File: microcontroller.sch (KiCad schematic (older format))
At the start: 15 parts

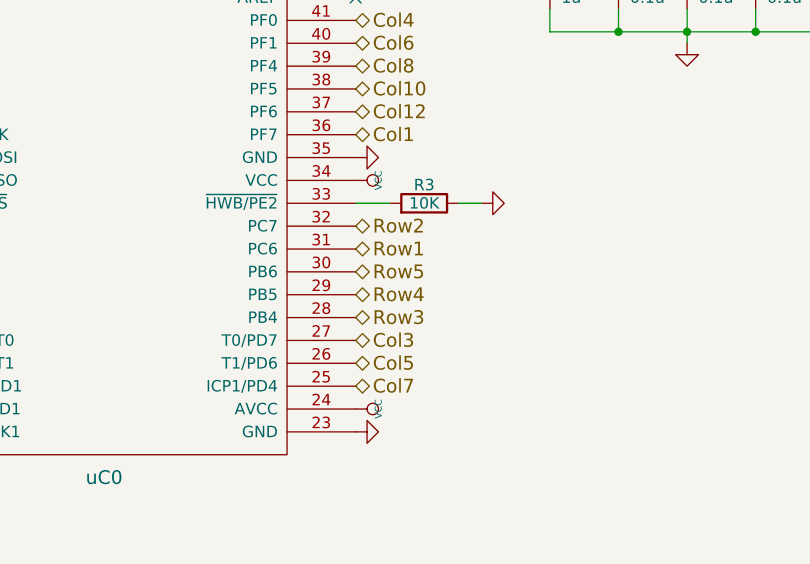
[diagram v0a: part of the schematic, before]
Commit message: Branch for finalizing the board.
TODO:
Swap to smaller components, finalize pads
Added footprints.pretty
Add RGB underglow
Added schematic library (keenkeeb.lib/dcm)
Remove SPI header (?)
Add test pads (?)
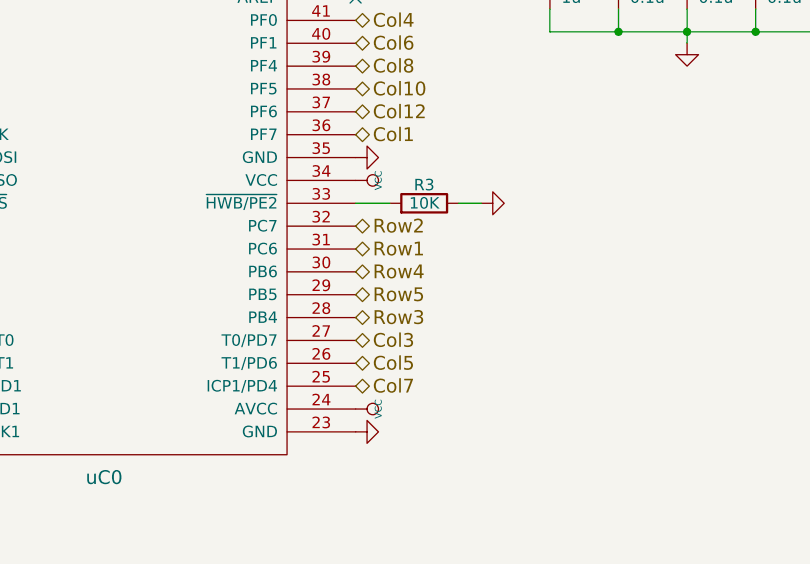
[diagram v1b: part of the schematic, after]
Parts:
- C0, C1, C2, C3, C4, C5, C6, C7: footprint Capacitors_SMD:C_0805_HandSoldering -> Capacitors_SMD:C_0805
- OSC0: footprint keyboard_parts:FA-238 -> footprints:OSC_EpsonFA238_SMD
- R0, R1, R2, R3: footprint Resistors_SMD:R_0805_HandSoldering -> Resistors_SMD:R_0805
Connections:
- net Row4: now also uC0.30 (PB6); no longer uC0.29 (PB5)
- net Row5: now also uC0.29 (PB5); no longer uC0.30 (PB6)
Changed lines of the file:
@@
 LIBS:contrib
 LIBS:valves
+LIBS:keenkeeb
 LIBS:keyboard_parts
 LIBS:pcb-cache
@@
 $Descr A4 11693 8268
 encoding utf-8
-Sheet 3 3
+Sheet 3 4
 Title ""
 Date ""
@@
 F 0 "R3" V 7480 4350 50  0000 C CNN
 F 1 "10K" V 7400 4350 50  0000 C CNN
-F 2 "Resistors_SMD:R_0805_HandSoldering" H 7400 4350 60  0001 C CNN
+F 2 "Resistors_SMD:R_0805" H 7400 4350 60  0001 C CNN
 F 3 "" H 7400 4350 60  0001 C CNN
 	1    7400 4350
@@
 F 0 "OSC0" H 3850 5300 60  0000 C CNN
 F 1 "XTAL_GND" H 3850 5000 60  0000 C CNN
-F 2 "keyboard_parts:FA-238" H 3850 5150 60  0001 C CNN
+F 2 "footprints:OSC_EpsonFA238_SMD" H 3850 5150 60  0001 C CNN
 F 3 "" H 3850 5150 60  0000 C CNN
 	1    3850 5150
@@
 F 0 "C0" V 4150 3800 50  0000 L CNN
 F 1 "1u" V 4150 3600 50  0000 L CNN
-F 2 "Capacitors_SMD:C_0805_HandSoldering" H 4200 3750 60  0001 C CNN
+F 2 "Capacitors_SMD:C_0805" H 4200 3750 60  0001 C CNN
 F 3 "" H 4200 3750 60  0001 C CNN
 	1    4200 3750
@@
 F 0 "R0" V 3130 4050 50  0000 C CNN
 F 1 "10K" V 3050 4050 50  0000 C CNN
-F 2 "Resistors_SMD:R_0805_HandSoldering" H 3050 4050 60  0001 C CNN
+F 2 "Resistors_SMD:R_0805" H 3050 4050 60  0001 C CNN
 F 3 "" H 3050 4050 60  0001 C CNN
 	1    3050 4050
@@
 F 0 "C2" H 4250 5500 50  0000 L CNN
 F 1 "22p" H 4250 5300 50  0000 L CNN
-F 2 "Capacitors_SMD:C_0805_HandSoldering" H 4200 5400 60  0001 C CNN
+F 2 "Capacitors_SMD:C_0805" H 4200 5400 60  0001 C CNN
 F 3 "" H 4200 5400 60  0001 C CNN
 	1    4200 5400
@@
 F 0 "C1" H 3350 5500 50  0000 L CNN
 F 1 "22p" H 3350 5300 50  0000 L CNN
-F 2 "Capacitors_SMD:C_0805_HandSoldering" H 3500 5400 60  0001 C CNN
+F 2 "Capacitors_SMD:C_0805" H 3500 5400 60  0001 C CNN
 F 3 "" H 3500 5400 60  0001 C CNN
 	1    3500 5400
@@
 F 0 "R1" V 4550 3450 50  0000 C CNN
 F 1 "22" V 4650 3450 50  0000 C CNN
-F 2 "Resistors_SMD:R_0805_HandSoldering" H 4650 3450 60  0001 C CNN
+F 2 "Resistors_SMD:R_0805" H 4650 3450 60  0001 C CNN
 F 3 "" H 4650 3450 60  0001 C CNN
 	1    4650 3450
@@
 F 0 "R2" V 4730 3550 50  0000 C CNN
 F 1 "22" V 4650 3550 50  0000 C CNN
-F 2 "Resistors_SMD:R_0805_HandSoldering" H 4650 3550 60  0001 C CNN
+F 2 "Resistors_SMD:R_0805" H 4650 3550 60  0001 C CNN
 F 3 "" H 4650 3550 60  0001 C CNN
 	1    4650 3550
@@
 F 0 "C3" H 8000 3450 50  0000 L CNN
 F 1 "1u" H 8000 3250 50  0000 L CNN
-F 2 "Capacitors_SMD:C_0805_HandSoldering" H 7950 3350 60  0001 C CNN
+F 2 "Capacitors_SMD:C_0805" H 7950 3350 60  0001 C CNN
 F 3 "" H 7950 3350 60  0001 C CNN
 	1    7950 3350
@@
 F 0 "C4" H 8300 3450 50  0000 L CNN
 F 1 "0.1u" H 8300 3250 50  0000 L CNN
-F 2 "Capacitors_SMD:C_0805_HandSoldering" H 8250 3350 60  0001 C CNN
+F 2 "Capacitors_SMD:C_0805" H 8250 3350 60  0001 C CNN
 F 3 "" H 8250 3350 60  0001 C CNN
 	1    8250 3350
@@
 F 0 "C5" H 8600 3450 50  0000 L CNN
 F 1 "0.1u" H 8600 3250 50  0000 L CNN
-F 2 "Capacitors_SMD:C_0805_HandSoldering" H 8550 3350 60  0001 C CNN
+F 2 "Capacitors_SMD:C_0805" H 8550 3350 60  0001 C CNN
 F 3 "" H 8550 3350 60  0001 C CNN
 	1    8550 3350
@@
 F 0 "C6" H 8900 3450 50  0000 L CNN
 F 1 "0.1u" H 8900 3250 50  0000 L CNN
-F 2 "Capacitors_SMD:C_0805_HandSoldering" H 8850 3350 60  0001 C CNN
+F 2 "Capacitors_SMD:C_0805" H 8850 3350 60  0001 C CNN
 F 3 "" H 8850 3350 60  0001 C CNN
 	1    8850 3350
@@
 F 0 "C7" H 9200 3450 50  0000 L CNN
 F 1 "0.1u" H 9200 3250 50  0000 L CNN
-F 2 "Capacitors_SMD:C_0805_HandSoldering" H 9150 3350 60  0001 C CNN
+F 2 "Capacitors_SMD:C_0805" H 9150 3350 60  0001 C CNN
 F 3 "" H 9150 3350 60  0001 C CNN
 	1    9150 3350
@@
 Text HLabel 7100 4850 2    60   BiDi ~ 0
 Row3
+Text HLabel 7100 4650 2    60   BiDi ~ 0
+Row4
 Text HLabel 7100 4750 2    60   BiDi ~ 0
-Row4
-Text HLabel 7100 4650 2    60   BiDi ~ 0
 Row5
 Text HLabel 4950 3250 0    60   Input ~ 0

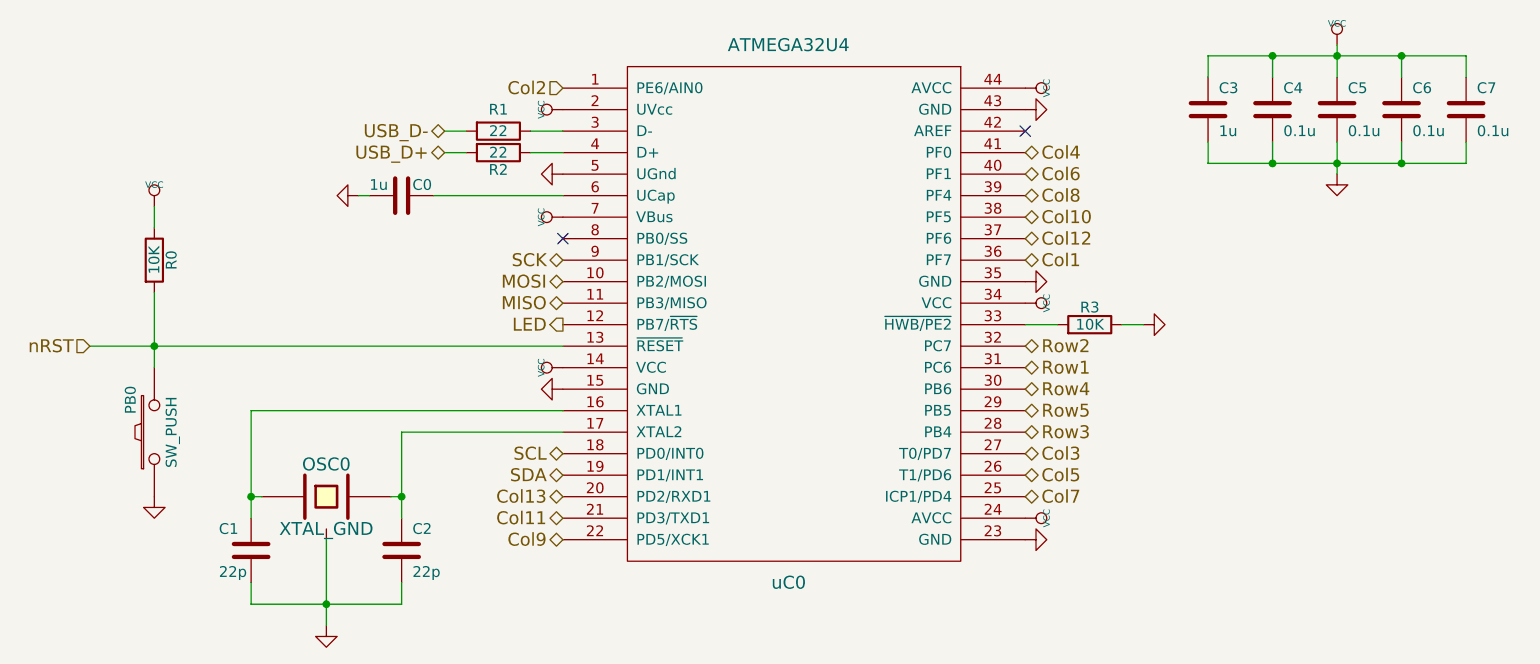
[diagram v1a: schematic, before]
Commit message: Added 0.1uF caps to LEDs
Added capacitors from Vcc to GND for WS2812s
Also changed some references
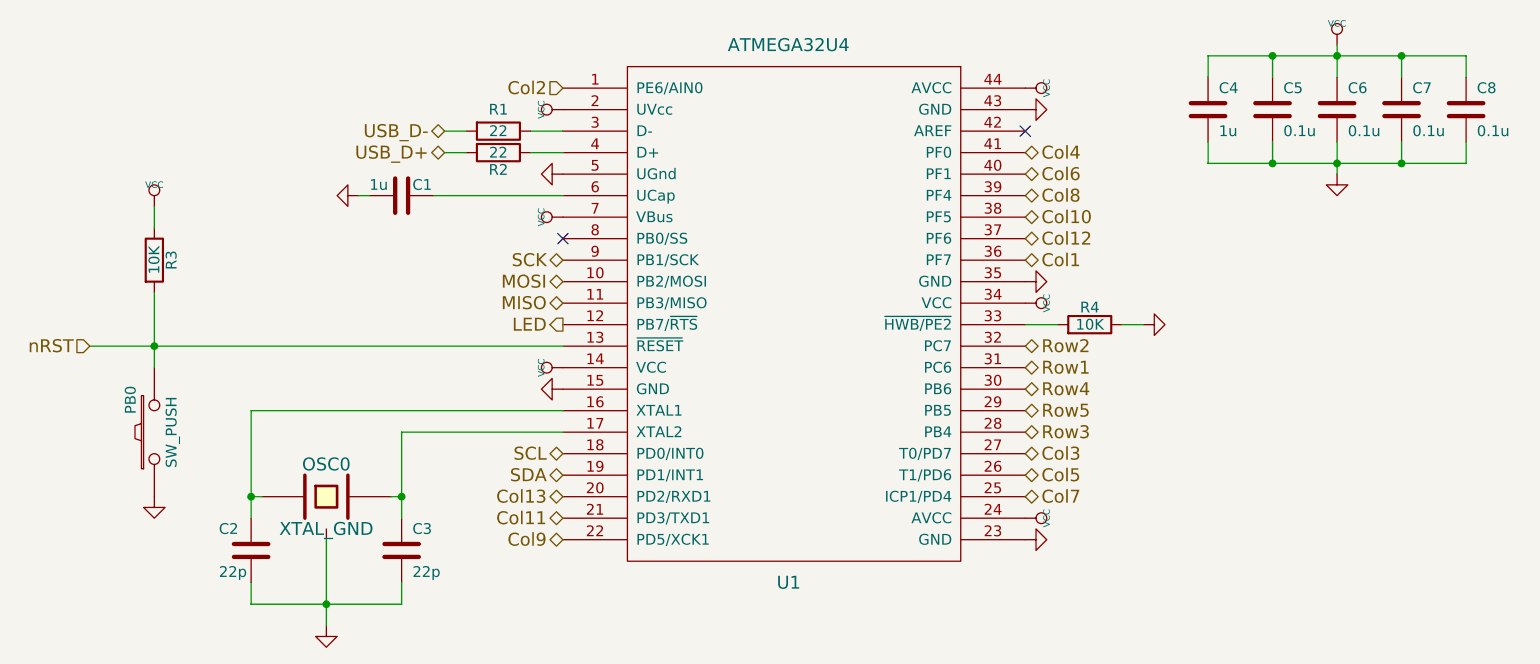
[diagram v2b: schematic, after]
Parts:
- renumbered uC0 to U1
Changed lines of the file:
@@
 P 7400 4350
 AR Path="/585B7C6B" Ref="R3"  Part="1"
-AR Path="/585C991A/585B7C6B" Ref="R3"  Part="1"
-F 0 "R3" V 7480 4350 50  0000 C CNN
+AR Path="/585C991A/585B7C6B" Ref="R4"  Part="1"
+F 0 "R4" V 7480 4350 50  0000 C CNN
 F 1 "10K" V 7400 4350 50  0000 C CNN
 F 2 "Resistors_SMD:R_0805" H 7400 4350 60  0001 C CNN
@@
 $EndComp
 $Comp
-L ATMEGA32U4 uC0
+L ATMEGA32U4 U1
 U 1 1 587B8230
 P 6000 4300
-F 0 "uC0" H 6000 3050 60  0000 C CNN
+F 0 "U1" H 6000 3050 60  0000 C CNN
 F 1 "ATMEGA32U4" H 6000 5550 60  0000 C CNN
 F 2 "Housings_QFP:TQFP-44_10x10mm_Pitch0.8mm" H 6000 4300 60  0001 C CNN
@@
 P 4200 3750
 AR Path="/587C0174" Ref="C0"  Part="1"
-AR Path="/585C991A/587C0174" Ref="C0"  Part="1"
-F 0 "C0" V 4150 3800 50  0000 L CNN
+AR Path="/585C991A/587C0174" Ref="C1"  Part="1"
+F 0 "C1" V 4150 3800 50  0000 L CNN
 F 1 "1u" V 4150 3600 50  0000 L CNN
 F 2 "Capacitors_SMD:C_0805" H 4200 3750 60  0001 C CNN
@@
 P 3050 4050
 AR Path="/587C0CFD" Ref="R0"  Part="1"
-AR Path="/585C991A/587C0CFD" Ref="R0"  Part="1"
-F 0 "R0" V 3130 4050 50  0000 C CNN
+AR Path="/585C991A/587C0CFD" Ref="R3"  Part="1"
+F 0 "R3" V 3130 4050 50  0000 C CNN
 F 1 "10K" V 3050 4050 50  0000 C CNN
 F 2 "Resistors_SMD:R_0805" H 3050 4050 60  0001 C CNN
@@
 P 4200 5400
 AR Path="/587C1927" Ref="C2"  Part="1"
-AR Path="/585C991A/587C1927" Ref="C2"  Part="1"
-F 0 "C2" H 4250 5500 50  0000 L CNN
+AR Path="/585C991A/587C1927" Ref="C3"  Part="1"
+F 0 "C3" H 4250 5500 50  0000 L CNN
 F 1 "22p" H 4250 5300 50  0000 L CNN
 F 2 "Capacitors_SMD:C_0805" H 4200 5400 60  0001 C CNN
@@
 P 3500 5400
 AR Path="/587C1976" Ref="C1"  Part="1"
-AR Path="/585C991A/587C1976" Ref="C1"  Part="1"
-F 0 "C1" H 3350 5500 50  0000 L CNN
+AR Path="/585C991A/587C1976" Ref="C2"  Part="1"
+F 0 "C2" H 3350 5500 50  0000 L CNN
 F 1 "22p" H 3350 5300 50  0000 L CNN
 F 2 "Capacitors_SMD:C_0805" H 3500 5400 60  0001 C CNN
@@
 P 7950 3350
 AR Path="/587C8FD9" Ref="C3"  Part="1"
-AR Path="/585C991A/587C8FD9" Ref="C3"  Part="1"
-F 0 "C3" H 8000 3450 50  0000 L CNN
+AR Path="/585C991A/587C8FD9" Ref="C4"  Part="1"
+F 0 "C4" H 8000 3450 50  0000 L CNN
 F 1 "1u" H 8000 3250 50  0000 L CNN
 F 2 "Capacitors_SMD:C_0805" H 7950 3350 60  0001 C CNN
@@
 P 8250 3350
 AR Path="/587C9145" Ref="C4"  Part="1"
-AR Path="/585C991A/587C9145" Ref="C4"  Part="1"
-F 0 "C4" H 8300 3450 50  0000 L CNN
+AR Path="/585C991A/587C9145" Ref="C5"  Part="1"
+F 0 "C5" H 8300 3450 50  0000 L CNN
 F 1 "0.1u" H 8300 3250 50  0000 L CNN
 F 2 "Capacitors_SMD:C_0805" H 8250 3350 60  0001 C CNN
@@
 P 8550 3350
 AR Path="/587C91CC" Ref="C5"  Part="1"
-AR Path="/585C991A/587C91CC" Ref="C5"  Part="1"
-F 0 "C5" H 8600 3450 50  0000 L CNN
+AR Path="/585C991A/587C91CC" Ref="C6"  Part="1"
+F 0 "C6" H 8600 3450 50  0000 L CNN
 F 1 "0.1u" H 8600 3250 50  0000 L CNN
 F 2 "Capacitors_SMD:C_0805" H 8550 3350 60  0001 C CNN
@@
 P 8850 3350
 AR Path="/587C9253" Ref="C6"  Part="1"
-AR Path="/585C991A/587C9253" Ref="C6"  Part="1"
-F 0 "C6" H 8900 3450 50  0000 L CNN
+AR Path="/585C991A/587C9253" Ref="C7"  Part="1"
+F 0 "C7" H 8900 3450 50  0000 L CNN
 F 1 "0.1u" H 8900 3250 50  0000 L CNN
 F 2 "Capacitors_SMD:C_0805" H 8850 3350 60  0001 C CNN
@@
 P 9150 3350
 AR Path="/587C92F4" Ref="C7"  Part="1"
-AR Path="/585C991A/587C92F4" Ref="C7"  Part="1"
-F 0 "C7" H 9200 3450 50  0000 L CNN
+AR Path="/585C991A/587C92F4" Ref="C8"  Part="1"
+F 0 "C8" H 9200 3450 50  0000 L CNN
 F 1 "0.1u" H 9200 3250 50  0000 L CNN
 F 2 "Capacitors_SMD:C_0805" H 9150 3350 60  0001 C CNN

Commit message: All switch columns wired.
Wired all switches in a column together and dropped the 10 existing
WS2812Bs in place.  Need to connect everything to controller.
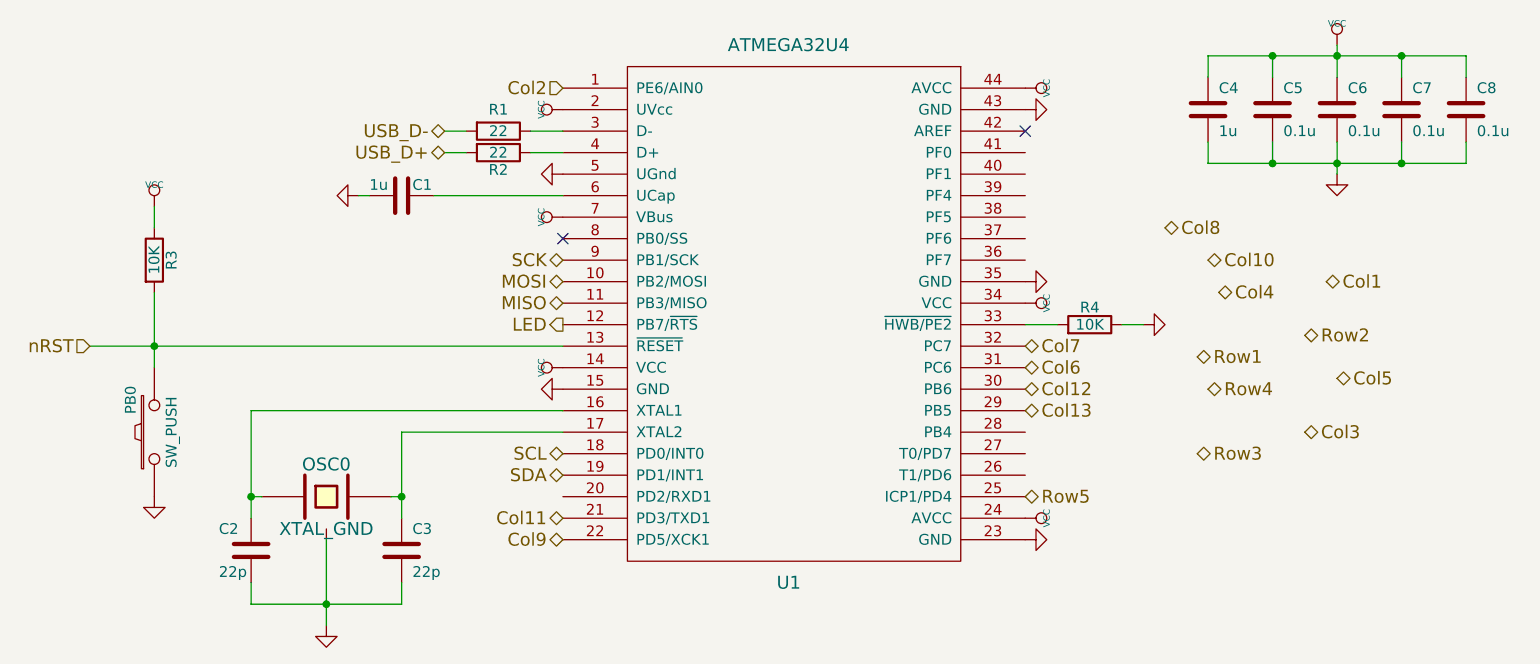
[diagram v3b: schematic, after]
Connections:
- net Col1: no longer U1.36 (PF7)
- net Col10: no longer U1.38 (PF5)
- net Col12: now also U1.30 (PB6); no longer U1.37 (PF6)
- net Col13: now also U1.29 (PB5); no longer U1.20 (PD2/RXD1)
- net Col3: no longer U1.27 (T0/PD7)
- net Col4: no longer U1.41 (PF0)
- net Col5: no longer U1.26 (T1/PD6)
- net Col6: now also U1.31 (PC6); no longer U1.40 (PF1)
- net Col7: now also U1.32 (PC7); no longer U1.25 (ICP1/PD4)
- net Col8: no longer U1.39 (PF4)
- net Row1: no longer U1.31 (PC6)
- net Row2: no longer U1.32 (PC7)
- net Row3: no longer U1.28 (PB4)
- net Row4: no longer U1.30 (PB6)
- net Row5: now also U1.25 (ICP1/PD4); no longer U1.29 (PB5)
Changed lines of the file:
@@
 	0    1    -1   0
 $EndComp
-Text HLabel 7100 3550 2    60   BiDi ~ 0
+Text HLabel 8000 4200 2    60   BiDi ~ 0
 Col4
-Text HLabel 7100 3650 2    60   BiDi ~ 0
+Text HLabel 7100 4550 2    60   BiDi ~ 0
 Col6
-Text HLabel 7100 3750 2    60   BiDi ~ 0
+Text HLabel 7750 3900 2    60   BiDi ~ 0
 Col8
-Text HLabel 7100 3950 2    60   BiDi ~ 0
+Text HLabel 7100 4650 2    60   BiDi ~ 0
 Col12
-Text HLabel 4950 5150 0    60   BiDi ~ 0
+Text HLabel 7100 4750 2    60   BiDi ~ 0
 Col13
 Text HLabel 4950 5250 0    60   BiDi ~ 0
@@
 Text HLabel 4950 5350 0    60   BiDi ~ 0
 Col9
-Text HLabel 7100 5150 2    60   BiDi ~ 0
+Text HLabel 7100 4450 2    60   BiDi ~ 0
 Col7
-Text HLabel 7100 5050 2    60   BiDi ~ 0
+Text HLabel 8550 4600 2    60   BiDi ~ 0
 Col5
-Text HLabel 7100 4950 2    60   BiDi ~ 0
+Text HLabel 8400 4850 2    60   BiDi ~ 0
 Col3
 $Comp
@@
 	8250 3500 8250 3600
 Connection ~ 8250 3600
-Text HLabel 7100 3850 2    60   BiDi ~ 0
+Text HLabel 7950 4050 2    60   BiDi ~ 0
 Col10
-Text HLabel 7100 4850 2    60   BiDi ~ 0
+Text HLabel 7900 4950 2    60   BiDi ~ 0
 Row3
-Text HLabel 7100 4650 2    60   BiDi ~ 0
+Text HLabel 7950 4650 2    60   BiDi ~ 0
 Row4
-Text HLabel 7100 4750 2    60   BiDi ~ 0
+Text HLabel 7100 5150 2    60   BiDi ~ 0
 Row5
 Text HLabel 4950 3250 0    60   Input ~ 0
 Col2
-Text HLabel 7100 4050 2    60   BiDi ~ 0
+Text HLabel 8500 4150 2    60   BiDi ~ 0
 Col1
-Text HLabel 7100 4450 2    60   BiDi ~ 0
+Text HLabel 8400 4400 2    60   BiDi ~ 0
 Row2
-Text HLabel 7100 4550 2    60   BiDi ~ 0
+Text HLabel 7900 4500 2    60   BiDi ~ 0
 Row1
 Text HLabel 4950 4950 0    60   BiDi ~ 0

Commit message: About half of rows/columns connected to microcontroller.
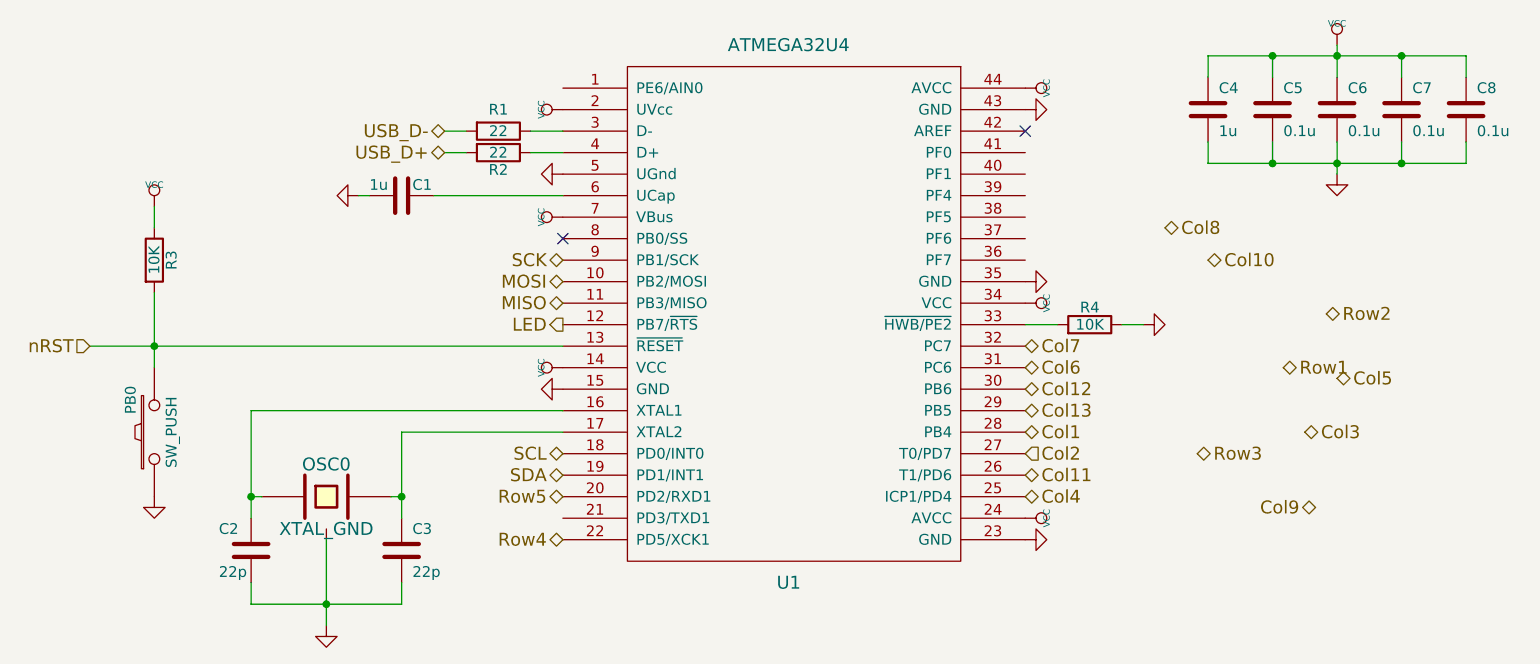
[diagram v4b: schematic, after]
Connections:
- net Col1: now also U1.28 (PB4)
- net Col11: now also U1.26 (T1/PD6); no longer U1.21 (PD3/TXD1)
- net Col2: now also U1.27 (T0/PD7); no longer U1.1 (PE6/AIN0)
- net Col4: now also U1.25 (ICP1/PD4)
- net Col9: no longer U1.22 (PD5/XCK1)
- net Row4: now also U1.22 (PD5/XCK1)
- net Row5: now also U1.20 (PD2/RXD1); no longer U1.25 (ICP1/PD4)
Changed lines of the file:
@@
 	0    1    -1   0
 $EndComp
-Text HLabel 8000 4200 2    60   BiDi ~ 0
+Text HLabel 7100 5150 2    60   BiDi ~ 0
 Col4
 Text HLabel 7100 4550 2    60   BiDi ~ 0
@@
 Text HLabel 7100 4750 2    60   BiDi ~ 0
 Col13
-Text HLabel 4950 5250 0    60   BiDi ~ 0
+Text HLabel 7100 5050 2    60   BiDi ~ 0
 Col11
-Text HLabel 4950 5350 0    60   BiDi ~ 0
+Text HLabel 8450 5200 0    60   BiDi ~ 0
 Col9
 Text HLabel 7100 4450 2    60   BiDi ~ 0
@@
 Text HLabel 7900 4950 2    60   BiDi ~ 0
 Row3
-Text HLabel 7950 4650 2    60   BiDi ~ 0
+Text HLabel 4950 5350 0    60   BiDi ~ 0
 Row4
-Text HLabel 7100 5150 2    60   BiDi ~ 0
+Text HLabel 4950 5150 0    60   BiDi ~ 0
 Row5
-Text HLabel 4950 3250 0    60   Input ~ 0
+Text HLabel 7100 4950 2    60   Input ~ 0
 Col2
-Text HLabel 8500 4150 2    60   BiDi ~ 0
+Text HLabel 7100 4850 2    60   BiDi ~ 0
 Col1
-Text HLabel 8400 4400 2    60   BiDi ~ 0
+Text HLabel 8500 4300 2    60   BiDi ~ 0
 Row2
-Text HLabel 7900 4500 2    60   BiDi ~ 0
+Text HLabel 8300 4550 2    60   BiDi ~ 0
 Row1
 Text HLabel 4950 4950 0    60   BiDi ~ 0
